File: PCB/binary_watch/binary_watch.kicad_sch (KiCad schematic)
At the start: 29 parts

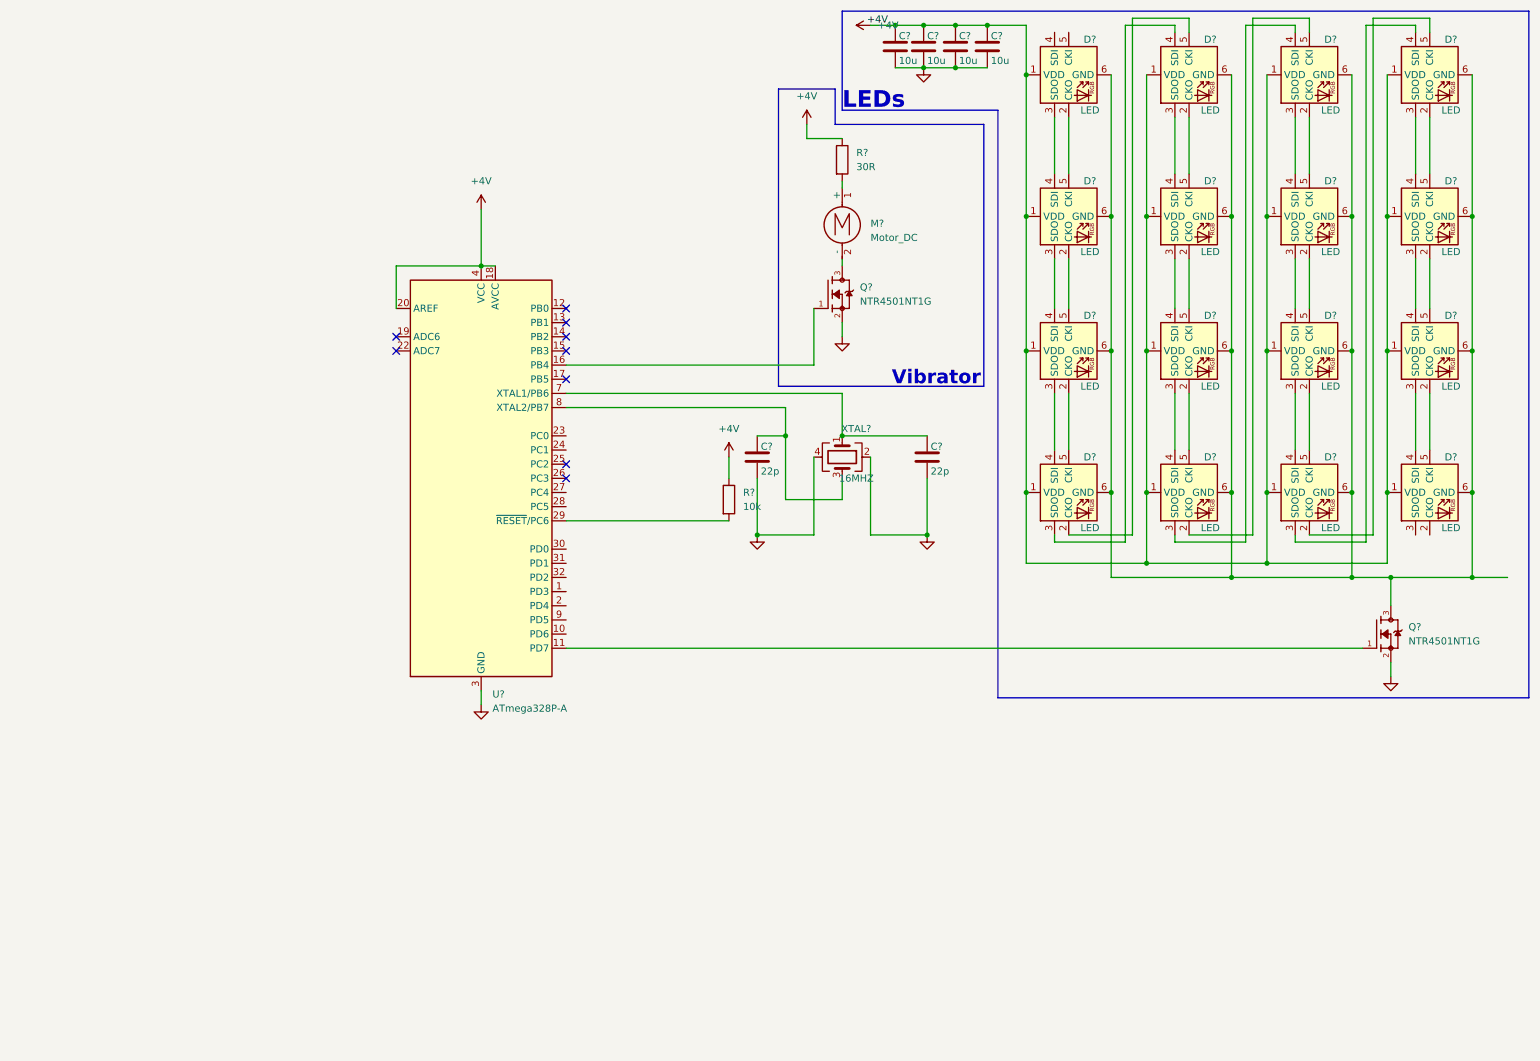
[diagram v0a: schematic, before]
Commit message: Added more sections on the schematics, added library files.
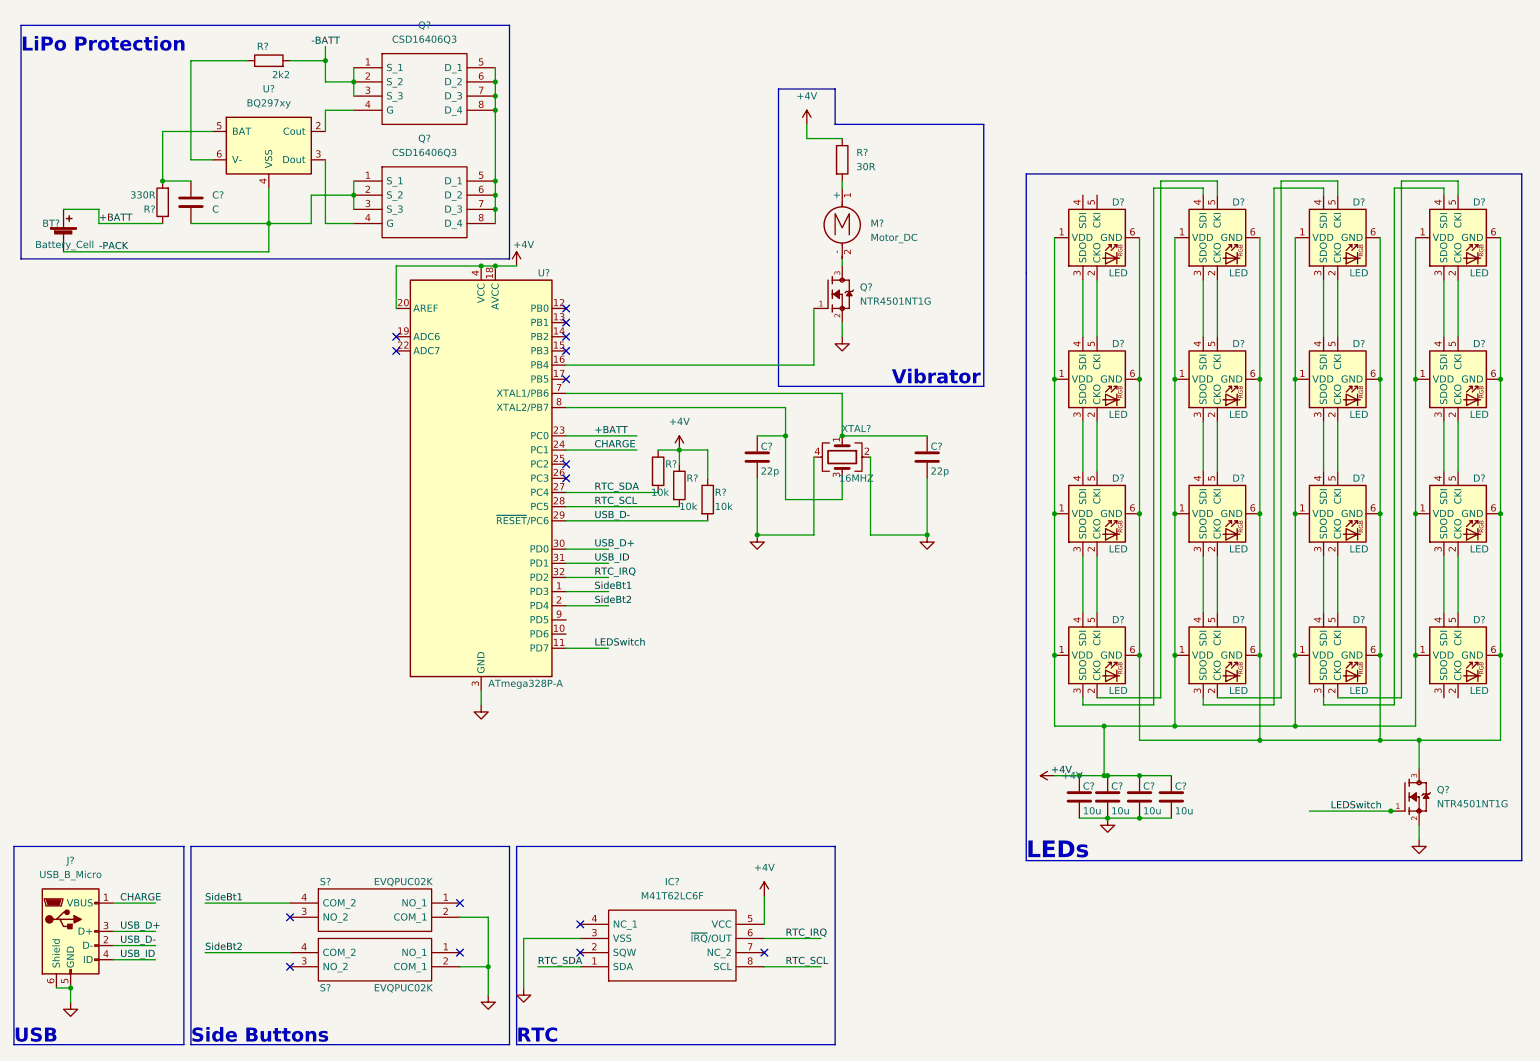
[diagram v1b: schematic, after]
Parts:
- removed C? (x4): 10u, symbol Device:C
- added BT?: Battery_Cell, symbol Device:Battery_Cell
- added C? (x4): 10u, symbol Device:C
- added C?: C, symbol Device:C
- added IC?: M41T62LC6F, M41T62LC6F, symbol M41T62LC6F:M41T62LC6F
- added J?: USB_B_Micro, symbol Connector:USB_B_Micro
- added Q? (x2): CSD16406Q3, DQG_VSON-CLIP, symbol CSD16406Q3:CSD16406Q3
- added R? (x2): 10k, symbol Device:R
- added R?: 330R, symbol Device:R
- added R?: 2k2, symbol Device:R
- added S? (x2): EVQPUC02K, EVQPUC02K, symbol EVQPUC02K:EVQPUC02K
- added U?: BQ297xy, Package_SON:WSON-6_1.5x1.5mm_P0.5mm, symbol Battery_Management:BQ297xy
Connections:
- net +4V: now also C?.1, C?.1, C?.1, C?.1, IC?.5 (VCC), R?.1, R?.1
- net GND: now also C?.2, C?.2, C?.2, C?.2, IC?.3 (VSS), J?.5 (GND), J?.6 (Shield), S?.2 (COM_1), S?.2 (COM_1)
- net SideBt1: now reaches U?.1 (PD3)
- net SideBt1: now also S?.4 (COM_2)
- net LEDSwitch: now reaches Q?.1, U?.11 (PD7)
- net SideBt2: now reaches U?.2 (PD4)
- net SideBt2: now also S?.4 (COM_2)
- net +BATT: now reaches U?.23 (PC0)
- net +BATT: now also BT?.1 (+), R?.1
- net CHARGE: now reaches U?.24 (PC1)
- net CHARGE: now also J?.1 (VBUS)
- net RTC_SDA: now reaches U?.27 (PC4)
- net RTC_SDA: now also IC?.1 (SDA), R?.2
- net RTC_SCL: now reaches U?.28 (PC5)
- net RTC_SCL: now also IC?.8 (SCL), R?.2
- net USB_D-: now reaches R?.2, U?.29 (~{RESET}/PC6)
- net USB_D-: now also J?.2 (D-)
- net USB_D+: now reaches U?.30 (PD0)
- net USB_D+: now also J?.3 (D+)
- net USB_ID: now reaches U?.31 (PD1)
- net USB_ID: now also J?.4 (ID)
- net RTC_IRQ: now reaches U?.32 (PD2)
- net RTC_IRQ: now also IC?.6 (~{IRQ}/OUT)
- new net: Q?.4 (G), U?.3 (Dout)
- new net: Q?.5 (D_1), Q?.5 (D_1), Q?.6 (D_2), Q?.6 (D_2), Q?.7 (D_3), Q?.7 (D_3), Q?.8 (D_4), Q?.8 (D_4)
- new net: Q?.4 (G), U?.2 (Cout)
- new net: C?.1, R?.2, U?.5 (BAT)
- new net: R?.1, U?.6 (V-)
- new net: Q?.1 (S_1), Q?.2 (S_2), Q?.3 (S_3), R?.2
- new net -PACK: BT?.2 (-), C?.2, Q?.1 (S_1), Q?.2 (S_2), Q?.3 (S_3), U?.4 (VSS)
- no-connect marks 9 -> 16
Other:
- note added: "LiPo Protection"
- note added: "RTC"
- note added: "Side Buttons"
- note added: "USB"
- company: (none) -> Umair Ahmadh
- title: (none) -> Binary Watch
- moved on the sheet: D?, Q?, R?

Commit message: Completed Schematics
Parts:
- removed C? (x2): 22p, symbol Device:C
- removed XTAL?: 16MHZ, symbol Device:Crystal_GND24
- added C? (x4): 10uF, symbol Device:C
- added C? (x2): 22p, symbol Device:C
- added L?: 4.7uH, LQH3NPN4R7MMEL, symbol Device:L
- added R?: 150k, symbol Device:R
- added R?: 1M, symbol Device:R
- added R?: 3k3, symbol Device:R
- added U?: MCP73831-2-OT, Package_TO_SOT_SMD:SOT-23-5, symbol Battery_Management:MCP73831-2-OT
- added U?: TPS61220DCK, Package_TO_SOT_SMD:Texas_R-PDSO-G6, symbol Regulator_Switching:TPS61220DCK
- added XTAL?: 16MHZ, symbol Device:Crystal_GND24
- C?: value C -> 0.1uF
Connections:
- net +4V: now also C?.1, R?.1, U?.4 (VOUT)
- net +BATT: now also C?.1, C?.1, L?.2, U?.1 (VIN), U?.3 (VBAT), U?.6 (EN)
- net CHARGE: now also C?.1, U?.4 (VDD)
- net GND: now also C?.2, C?.2, C?.2, C?.2, C?.2, C?.2, R?.1, R?.2, U?.2 (VSS), U?.3 (GND), XTAL?.2, XTAL?.4
- net LED_DIN: now reaches U?.10 (PD6)
- net LED_DIN: now also D?.4 (SDI)
- net Vibrator: now reaches Q?.1, U?.16 (PB4)
- net XTAL1: now reaches U?.7 (XTAL1/PB6)
- net XTAL1: now also C?.1, XTAL?.1
- net XTAL2: now reaches U?.8 (XTAL2/PB7)
- net XTAL2: now also C?.1, XTAL?.3
- net LED_CLK: now reaches U?.9 (PD5)
- net LED_CLK: now also D?.5 (CKI)
- new net: R?.1, R?.2, U?.2 (FB)
- new net: R?.2, U?.5 (PROG)
- new net: L?.1, U?.5 (L)
- no-connect marks 16 -> 17
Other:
- note added: "Charge"
- note added: "DC-DC"
- note added: "MCU"
- note added: "Oscillator"
- moved on the sheet: M?, Q?, R?, U?

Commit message: component placement done
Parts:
- removed XTAL?: 16MHZ, symbol Device:Crystal_GND24
- added J3: Conn_02x03_Odd_Even, Connector_PinHeader_2.54mm:PinHeader_2x03_P2.54mm_Horizontal, symbol Connector_Generic:Conn_02x03_Odd_Even
- added Y1: ECS-160-12-33-AGN-TR, ECS-160-12-33-AGN-TR:XTAL_ECS-160-12-33-AGN-TR, symbol ECS-160-12-33-AGN-TR:ECS-160-12-33-AGN-TR
- C1, C10, C11, C2, C3, C4, C5, C6, C7, C8, C9: renamed from C?; footprint (none) -> Capacitor_SMD:C_0603_1608Metric
- J1: renamed from BT?; footprint (none) -> Battery:Battery_Panasonic_CR1025-VSK_Vertical_CircularHoles
- J2: renamed from J?; footprint (none) -> Connector_USB:USB_Micro-B_Amphenol_10118194_Horizontal
- L1: renamed from L?; footprint LQH3NPN4R7MMEL -> Inductor_SMD:L_Vishay_IHLP-1212
- M1: renamed from M?; footprint (none) -> Connector_PinHeader_2.54mm:PinHeader_1x02_P2.54mm_Horizontal
- Q1, Q4: renamed from Q?; footprint SOT95P237X111-3N -> Package_TO_SOT_SMD:SOT-23
- Q2, Q3: renamed from Q?; footprint DQG_VSON-CLIP -> CSD16406Q3:TRANS_CSD16406Q3
- R1, R2, R3, R4, R5, R6, R7, R8, R9: renamed from R?; footprint (none) -> Resistor_SMD:R_0603_1608Metric
- S1, S2: renamed from S?; footprint EVQPUC02K -> EVQPUC02K:EVQPUC02K
- U5: renamed from IC?; footprint M41T62LC6F -> M41T62LC6F:M41T62LC6F
- gave numbers to parts that had none: 20
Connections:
- net +4V: now also J3.1 (Pin_1)
- net GND: now also Q2.1 (S_1), Q2.2 (S_2), Q2.3 (S_3), R2.2, J3.6 (Pin_6), Y1.2 (GND), Y1.4 (GND)
- net XTAL1: now also Y1.1 (IN/OUT)
- net XTAL2: now also Y1.3 (OUT/IN)
- net MOSI: now reaches U1.15 (PB3)
- net MOSI: now also J3.2 (Pin_2)
- net SCK: now reaches U1.17 (PB5)
- net SCK: now also J3.3 (Pin_3)
- net USB_D- renamed CS
- net CS: now also J3.4 (Pin_4)
- net Vibrator renamed MISO
- net MISO: now also J3.5 (Pin_5)
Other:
- moved on the sheet: R7, R8, R9, U1
